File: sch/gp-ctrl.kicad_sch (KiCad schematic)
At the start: 10 parts

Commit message: more components
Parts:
- added A? (x2): SolderJumper_2_Open, Jumper:SolderJumper-2_P1.3mm_Open_TrianglePad1.0x1.5mm, symbol Jumper:SolderJumper_2_Open
- added D?: SS34, Diode_SMD:D_SMA, symbol Device:D_Schottky
- added Q?: 2N7002P, Package_TO_SOT_SMD:SOT-23, symbol Transistor_FET:2N7002
- added R? (x4): 10k, Resistor_SMD:R_0402_1005Metric_Pad0.72x0.64mm_HandSolder, symbol Device:R
- J?: LCSC (none) -> C3975165
- JP? (x3): footprint Jumper:SolderJumper-2_P1.3mm_Open_Pad1.0x1.5mm -> gpctrl:power_jumper
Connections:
- net +3V3: now also Q?.1 (G), R?.2
- net +5V: now also A?.2 (B), A?.2 (B), D?.1 (K), R?.2
- net GND: now also J?.14 (Pin_14), J?.20 (Pin_20), J?.30 (Pin_30), J?.34 (Pin_34), U?.6 (GND), R?.1, R?.1
- net at U?.1 (A1): now also A?.1 (A), R?.2, R?.2
- net at U?.2 (A0): now also A?.1 (A)
- net SDA1: now reaches U?.3 (SDA)
- net SCL1: now reaches U?.4 (SCL)
- net UART_P_RX: now reaches J?.10 (Pin_10)
- net SH_GP23_IMU: now reaches J?.16 (Pin_16)
- net SH_PGP24_IMU: now reaches J?.18 (Pin_18)
- net at J?.2 (Pin_2): now also J?.4 (Pin_4), D?.2 (A)
- net SDA_SH: now reaches J?.3 (Pin_3)
- net SCL_SH: now reaches J?.5 (Pin_5)
- net UART_P_TX: now reaches J?.8 (Pin_8)
- new net: Q?.3 (D), R?.1
- new net: Q?.2 (S), R?.1
- no-connect marks 0 -> 2
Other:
- sheet controller ports: added +5V, 3V3, GND, GPIO0, GPIO1, GPIO10, GPIO11, GPIO12, GPIO13, GPIO14, GPIO15, GPIO16, GPIO17, GPIO18, GPIO19, GPIO2, GPIO20, GPIO21, GPIO22, GPIO23_PICO_NO, GPIO24_PICO_NO, GPIO25_LED, GPIO26_ADC0, GPIO27_ADC1, GPIO28_ADC2, GPIO29_ADC3, GPIO3, GPIO4, GPIO5, GPIO6, GPIO7, GPIO8, GPIO9, RUN, SWCLK, SWD; removed none
- moved on the sheet: J?, JP?, K?, R?, U?

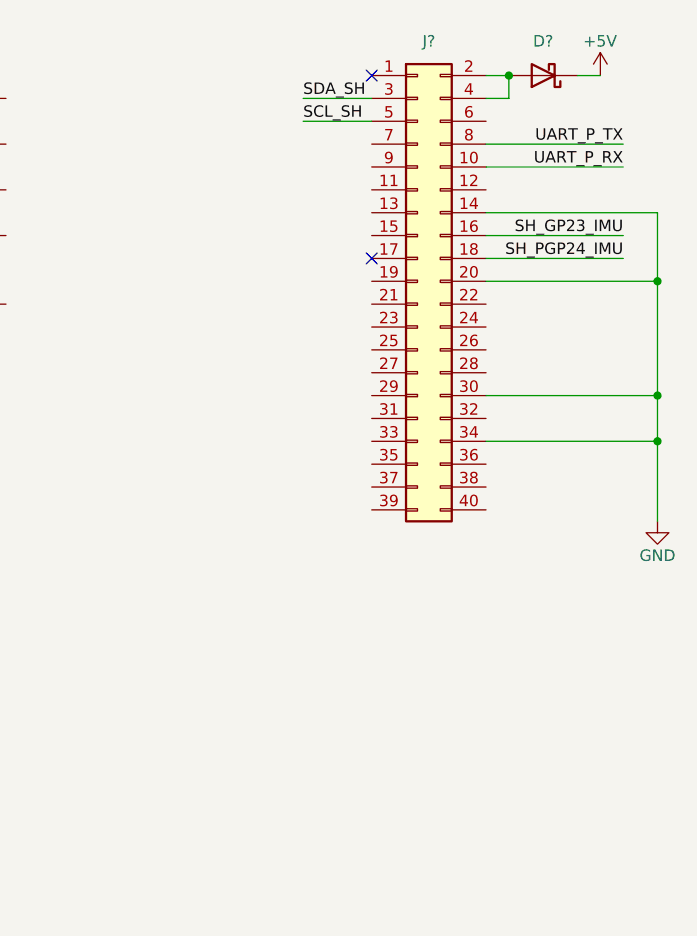
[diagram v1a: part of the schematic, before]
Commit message: updated downstream to sense hat connector
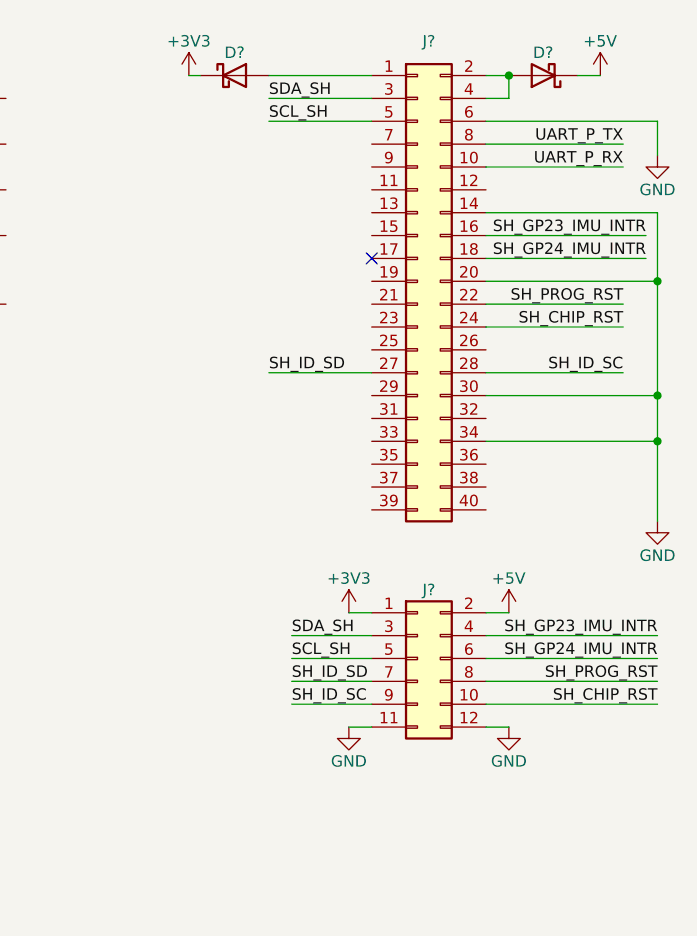
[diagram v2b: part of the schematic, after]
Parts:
- added D?: SS34, Diode_SMD:D_SMA, symbol Device:D_Schottky
- added J?: Conn_02x06_Odd_Even, Connector_PinHeader_2.54mm:PinHeader_2x06_P2.54mm_Horizontal, symbol Connector_Generic:Conn_02x06_Odd_Even
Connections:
- net +3V3: now also D?.1 (K), J?.1 (Pin_1)
- net +5V: now also J?.2 (Pin_2)
- net GND: now also J?.6 (Pin_6), J?.11 (Pin_11), J?.12 (Pin_12)
- net SCL_SH: now also J?.5 (Pin_5)
- net SDA_SH: now also J?.3 (Pin_3)
- net at J?.1 (Pin_1): now also D?.2 (A)
- net SH_PROG_RST: now reaches J?.22 (Pin_22)
- net SH_PROG_RST: now also J?.8 (Pin_8)
- net SH_CHIP_RST: now reaches J?.24 (Pin_24)
- net SH_CHIP_RST: now also J?.10 (Pin_10)
- net SH_ID_SD: now reaches J?.27 (Pin_27)
- net SH_ID_SD: now also J?.7 (Pin_7)
- net SH_ID_SC: now reaches J?.28 (Pin_28)
- net SH_ID_SC: now also J?.9 (Pin_9)
- net SH_GP23_IMU renamed SH_GP23_IMU_INTR
- net SH_GP23_IMU_INTR: now also J?.4 (Pin_4)
- net SH_PGP24_IMU renamed SH_GP24_IMU_INTR
- net SH_GP24_IMU_INTR: now also J?.6 (Pin_6)
- no-connect marks 2 -> 1

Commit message: sch update
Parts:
- added Q? (x3): 2N7002P, Package_TO_SOT_SMD:SOT-23, symbol Transistor_FET:2N7002
- added R? (x6): 10k, Resistor_SMD:R_0402_1005Metric_Pad0.72x0.64mm_HandSolder, symbol Device:R
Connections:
- net +3V3: now also Q?.1 (G), Q?.1 (G), Q?.1 (G), R?.2, R?.2, R?.2
- net +5V: now also R?.2, R?.2, R?.2
- new net: Q?.3 (D), R?.1 (x3)
- new net: Q?.2 (S), R?.1 (x3)
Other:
- note added: "1. No Board Sense"
- note added: "2. Board Sense Only"
- note added: "3. External Sense Only"
- moved on the sheet: A?, J?, JP?, K?, Q?, R?, U?

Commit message: sch update
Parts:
- removed K?: Relay_DPDT_Panasonic_AGQ200A4H, usb_xwitch:Relay_DPDT_Panasonic_AGQ200A4H, symbol usb_xwitch:Relay_DPDT_Panasonic_AGQ200A4H
- added J? (x2): 3.5mm_01x03, TerminalBlock_4Ucon:TerminalBlock_4Ucon_1x03_P3.50mm_Horizontal, symbol Connector:Screw_Terminal_01x03
- added J? (x2): DNP, Connector_PinHeader_2.54mm:PinHeader_1x03_P2.54mm_Vertical, symbol Connector_Generic:Conn_01x03
- added K? (x2): Relay_DPDT_Panasonic_AGQ200A4H, usb_xwitch:Relay_DPDT_Panasonic_AGQ200A4H, symbol usb_xwitch:Relay_DPDT_Panasonic_AGQ200A4H
- added Q? (x2): IRLML6244, Package_TO_SOT_SMD:SOT-23, symbol Transistor_FET:IRLML0030
- added R? (x2): 100K, Resistor_SMD:R_0603_1608Metric_Pad0.98x0.95mm_HandSolder, symbol Device:R
- added R?: 33K, Resistor_SMD:R_0603_1608Metric_Pad0.98x0.95mm_HandSolder, symbol Device:R
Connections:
- net at Q?.1 (G): now also Q?.3 (D), R?.1
- net at Q?.3 (D), R?.1: now also Q?.1 (G) (x3)
- new net: J?.3 (Pin_3), K?.2 (x2)
- new net: J?.1 (Pin_1), K?.3 (x2)
- new net: J?.2 (Pin_2), K?.4 (x2)
- new net: J?.2 (Pin_2), K?.5 (x2)
- new net: J?.1 (Pin_1), K?.6 (x2)
- new net: J?.3 (Pin_3), K?.7 (x2)
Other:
- note added: "Tri-Mode Current Sensor"
- moved on the sheet: Q?

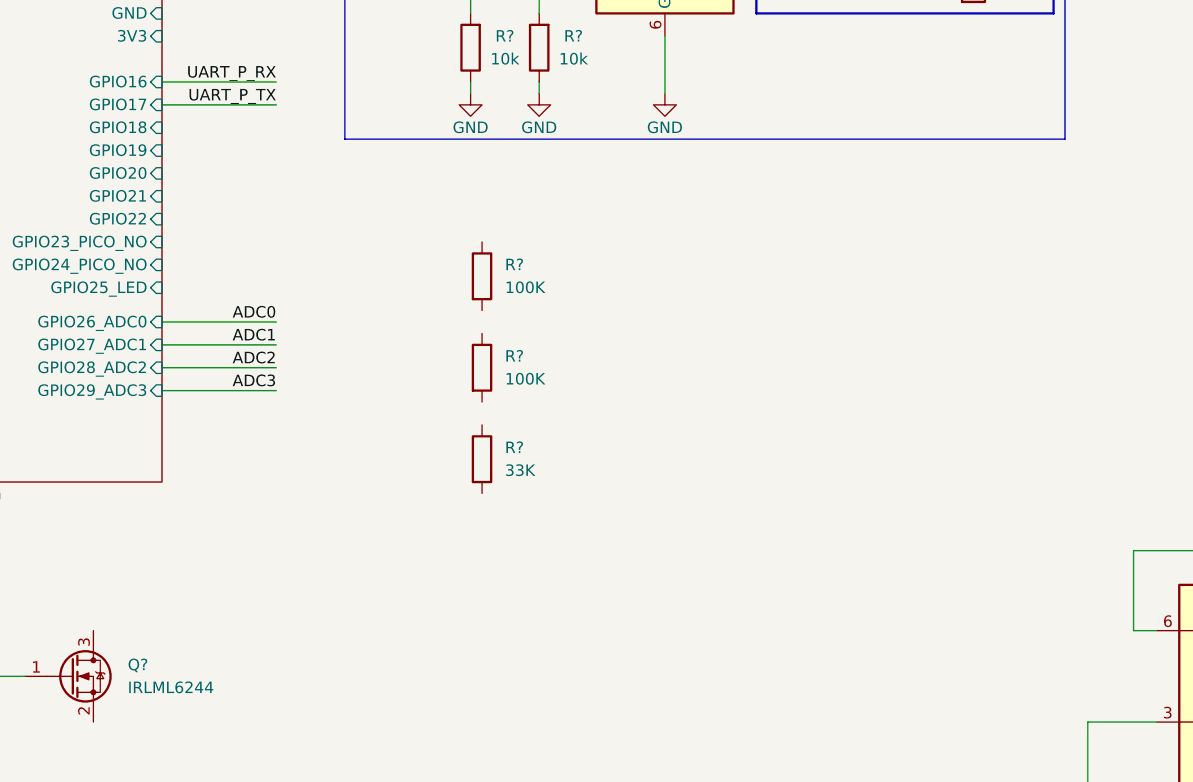
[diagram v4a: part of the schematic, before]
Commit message: adc added
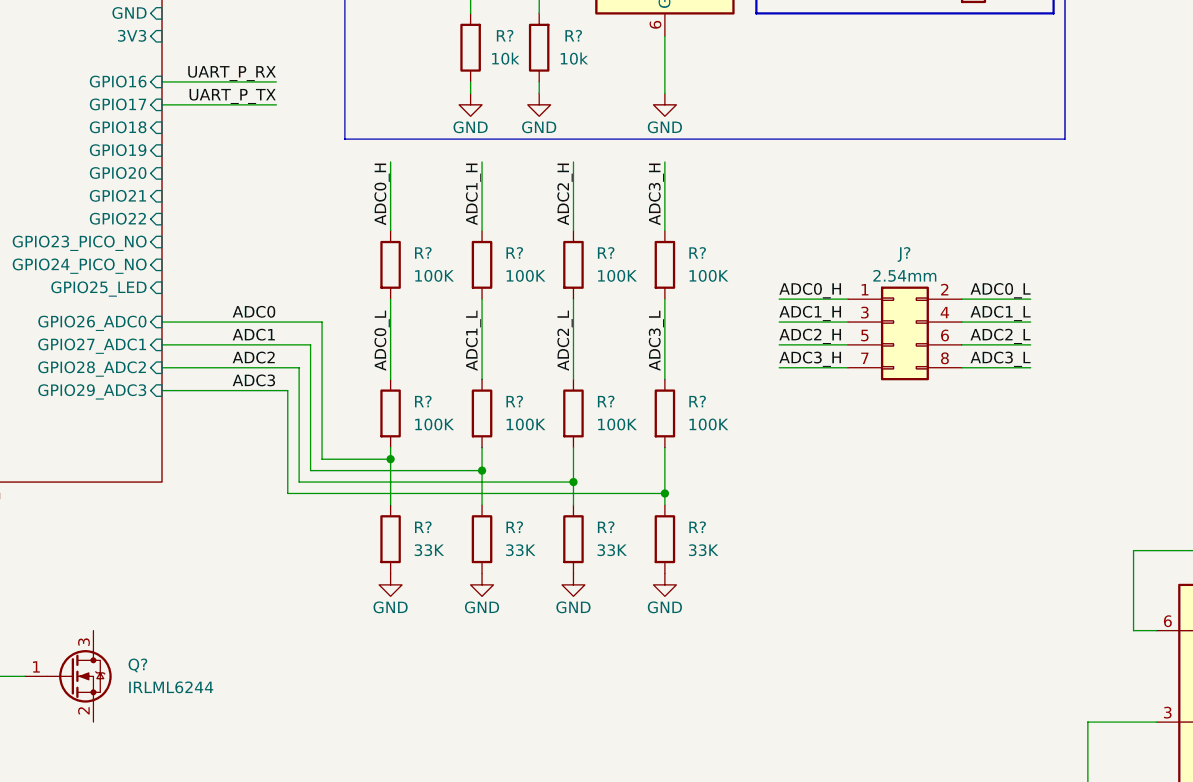
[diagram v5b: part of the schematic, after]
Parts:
- added J?: 2.54mm, Connector_PinHeader_2.54mm:PinHeader_2x04_P2.54mm_Vertical, symbol Connector_Generic:Conn_02x04_Odd_Even
- added R? (x6): 100K, Resistor_SMD:R_0603_1608Metric_Pad0.98x0.95mm_HandSolder, symbol Device:R
- added R? (x3): 33K, Resistor_SMD:R_0603_1608Metric_Pad0.98x0.95mm_HandSolder, symbol Device:R
- R? (x2): LCSC (none) -> C25803
- R?: LCSC (none) -> C4216
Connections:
- net ADC0: now also R?.1, R?.2
- net ADC1: now also R?.1, R?.2
- net ADC2: now also R?.1, R?.2
- net ADC3: now also R?.1, R?.2
- net GND: now also R?.2, R?.2, R?.2, R?.2
- net ADC3_L: now reaches R?.1
- net ADC3_L: now also R?.2, J?.8 (Pin_8)
- net ADC3_H: now reaches R?.1
- net ADC3_H: now also J?.7 (Pin_7)
- new net ADC0_H: J?.1 (Pin_1), R?.1
- new net ADC0_L: J?.2 (Pin_2), R?.1, R?.2
- new net ADC1_H: J?.3 (Pin_3), R?.1
- new net ADC1_L: J?.4 (Pin_4), R?.1, R?.2
- new net ADC2_H: J?.5 (Pin_5), R?.1
- new net ADC2_L: J?.6 (Pin_6), R?.1, R?.2
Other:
- moved on the sheet: R?

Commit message: sch and pcb layout update
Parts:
- removed J?: 3.5mm_01x03, TerminalBlock_4Ucon:TerminalBlock_4Ucon_1x03_P3.50mm_Horizontal, symbol Connector:Screw_Terminal_01x03
- removed J?: DNP, Connector_PinHeader_2.54mm:PinHeader_1x03_P2.54mm_Vertical, symbol Connector_Generic:Conn_01x03
- removed K?: Relay_DPDT_Panasonic_AGQ200A4H, usb_xwitch:Relay_DPDT_Panasonic_AGQ200A4H, symbol usb_xwitch:Relay_DPDT_Panasonic_AGQ200A4H
- added A1, A2: SolderJumper_2_Open, Jumper:SolderJumper-2_P1.3mm_Open_TrianglePad1.0x1.5mm, symbol Jumper:SolderJumper_2_Open
- added C1, C2: 100n, Resistor_SMD:R_0402_1005Metric_Pad0.72x0.64mm_HandSolder, symbol Device:C
- added D3, D4: B5819W SL, Diode_SMD:D_SOD-123, symbol Diode:BAT48ZFILM
- added H1, H2, H3, H4: RPI Mounting Hole, MountingHole:MountingHole_3.2mm_M3_Pad, symbol Mechanical:MountingHole
- added J1: DNP, Connector_PinHeader_2.54mm:PinHeader_1x02_P2.54mm_Vertical, symbol Connector_Generic:Conn_01x02
- added J10, J11, J13: 3.5mm, TerminalBlock_4Ucon:TerminalBlock_4Ucon_1x03_P3.50mm_Horizontal, symbol Connector:Screw_Terminal_01x03
- added J15: DNP, Connector_PinHeader_2.54mm:PinHeader_1x03_P2.54mm_Vertical_SMD_Pin1Left, symbol Connector_Generic:Conn_01x03
- added J16: Conn_02x06_Odd_Even, Connector_PinHeader_2.54mm:PinHeader_2x06_P2.54mm_Vertical, symbol Connector_Generic:Conn_02x06_Odd_Even
- added J5, J6, J9: 2.54mm, Connector_PinHeader_2.54mm:PinHeader_2x04_P2.54mm_Vertical, symbol Connector_Generic:Conn_02x04_Odd_Even
- added K2: Relay_DPDT_Panasonic_AGQ200A4H, usb_xwitch:Relay_DPDT_Panasonic_AGQ200A4H, symbol usb_xwitch:Relay_DPDT_Panasonic_AGQ200A4H
- added Q10, Q5, Q6, Q9: 2N7002P, Package_TO_SOT_SMD:SOT-23, symbol Transistor_FET:2N7002
- added R1, R2, R22, R27: 10K, Resistor_SMD:R_0603_1608Metric_Pad0.98x0.95mm_HandSolder, symbol Device:R
- added R3, R4: 100K, Resistor_SMD:R_0603_1608Metric_Pad0.98x0.95mm_HandSolder, symbol Device:R
- added SW1, SW2: C2689642, usb_xwitch:SW_SPST_CK_PTS636_SP43_SMTR, symbol Switch:SW_SPST
- J12: renamed from J?; value 3.5mm_01x03 -> 3.5mm
- J14: renamed from J?; footprint Connector_PinHeader_2.54mm:PinHeader_1x03_P2.54mm_Vertical -> Connector_PinHeader_2.54mm:PinHeader_1x03_P2.54mm_Vertical_SMD_Pin1Left
- J7: renamed from J?; LCSC (none) -> C225519
- J8: renamed from J?; value Conn_02x06_Odd_Even -> DNP; footprint Connector_PinHeader_2.54mm:PinHeader_2x06_P2.54mm_Horizontal -> Connector_PinHeader_2.54mm:PinHeader_2x06_P2.54mm_Vertical
- gave numbers to parts that had none: 42
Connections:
- net +12V: now also J9.1 (Pin_1), J9.2 (Pin_2)
- net +3V3: now also J5.7 (Pin_7), J5.8 (Pin_8), J6.7 (Pin_7), J6.8 (Pin_8), J9.5 (Pin_5), J9.6 (Pin_6), R1.1, R2.1, R22.1, R27.1
- net +5V: now also K1.1, D3.1 (K), D4.1 (K), J16.10 (Pin_10), J16.12 (Pin_12), J16.2 (Pin_2), J16.4 (Pin_4), J16.6 (Pin_6), J16.8 (Pin_8), J9.3 (Pin_3), J9.4 (Pin_4), K2.1
- net ADC0_H: now also J10.1 (Pin_1)
- net ADC0_L: now also J10.2 (Pin_2)
- net ADC1_H: now also J11.1 (Pin_1)
- net ADC1_L: now also J11.2 (Pin_2)
- net GND: now also J3.13 (Pin_13), J3.19 (Pin_19), J3.29 (Pin_29), J3.33 (Pin_33), J3.5 (Pin_5), Q12.2 (S), Q2.2 (S), Q4.2 (S), Q8.2 (S), C1.2, C2.2, J10.3 (Pin_3), J11.3 (Pin_3), J5.5 (Pin_5), J5.6 (Pin_6), J6.5 (Pin_5), J6.6 (Pin_6), J9.7 (Pin_7), J9.8 (Pin_8), Q10.2 (S), Q5.2 (S), Q6.2 (S), Q9.2 (S), R3.2, R4.2, SW1.1 (A), SW2.1 (A); no longer J3.14 (Pin_14), J3.20 (Pin_20), J3.30 (Pin_30), J3.34 (Pin_34), J3.6 (Pin_6)
- net SCL1: now also A1.1 (A), J5.2 (Pin_2), R2.2, R4.1
- net SCL_SH: now also J3.6 (Pin_6), A1.2 (B), J5.1 (Pin_1); no longer J3.5 (Pin_5)
- net SDA1: now also A2.1 (A), J5.4 (Pin_4), R1.2, R3.1
- net SDA_SH: now also J3.4 (Pin_4), A2.2 (B), J5.3 (Pin_3); no longer J3.3 (Pin_3)
- net SH_CHIP_RST: now also J3.23 (Pin_23); no longer J3.24 (Pin_24)
- net SH_GP23_IMU_INTR: now also J3.15 (Pin_15); no longer J3.16 (Pin_16)
- net SH_GP24_IMU_INTR: now also J3.17 (Pin_17); no longer J3.18 (Pin_18)
- net SH_ID_SC: now also J3.27 (Pin_27); no longer J3.28 (Pin_28)
- net SH_ID_SD: now also J3.28 (Pin_28); no longer J3.27 (Pin_27)
- net SH_PROG_RST: now also J3.21 (Pin_21); no longer J3.22 (Pin_22)
- net UART_P_RX: now also J3.9 (Pin_9); no longer J3.10 (Pin_10)
- net UART_P_TX: now also J3.7 (Pin_7); no longer J3.8 (Pin_8)
- net GP3: now reaches Q8.3 (D)
- net GP3: now also J16.5 (Pin_5)
- net at A4.1 (A), R6.2, U1.1 (A1): no longer R7.2
- net at A3.1 (A), U1.2 (A0): now also R7.2
- net GP2: now reaches Q4.3 (D)
- net GP2: now also J16.3 (Pin_3)
- net GP1: now reaches Q2.3 (D)
- net GP1: now also J16.1 (Pin_1)
- net CTGP4: now reaches Q11.2 (S), R28.1
- net CTGP2: now reaches Q3.2 (S), R23.1
- net CTGP1: now reaches Q1.2 (S), R20.1
- net at D1.2 (A): now also J3.2 (Pin_2); no longer J3.1 (Pin_1)
- net NC_RL_P0: now reaches J14.3 (Pin_3), K1.2
- net COM_RL_P0: now reaches J14.1 (Pin_1), K1.3
- net NO_RL_P0: now reaches J14.2 (Pin_2), K1.4
- net NO_RL_T0: now reaches J12.2 (Pin_2), K1.5
- net COM_RL_T0: now reaches J12.1 (Pin_1), K1.6
- net NC_RL_T0: now reaches J12.3 (Pin_3), K1.7
- net RL1: now reaches K1.8
- net RL1: now also D3.2 (A), Q5.3 (D)
- net CTGP3: now reaches Q7.2 (S), R25.1
- net GP4: now reaches Q12.3 (D)
- net GP4: now also J16.7 (Pin_7)
- new net: D2.2 (A), J3.1 (Pin_1), J3.3 (Pin_3)
- new net BTN1: C1.1, R22.2, SW1.2 (B)
- new net BTN2: C2.1, R27.2, SW2.2 (B)
- new net COM_RL_P1: J15.1 (Pin_1), K2.3
- new net COM_RL_T1: J13.1 (Pin_1), K2.6
- new net CTGP5: Q6.1 (G)
- new net CTGP6: Q10.1 (G)
- new net GP5: J16.9 (Pin_9), Q6.3 (D)
- new net GP6: J16.11 (Pin_11), Q10.3 (D)
- new net MI_RX: J6.1 (Pin_1)
- new net MO_TX: J6.2 (Pin_2)
- new net NC_RL_P1: J15.3 (Pin_3), K2.2
- new net NC_RL_T1: J13.3 (Pin_3), K2.7
- new net NO_RL_P1: J15.2 (Pin_2), K2.4
- new net NO_RL_T1: J13.2 (Pin_2), K2.5
- new net RL1_CTL: Q5.1 (G)
- new net RL2: D4.2 (A), K2.8, Q9.3 (D)
- new net RL2_CTL: Q9.1 (G)
- new net SCK_SP: J6.3 (Pin_3)
- new net SCL_CS: J6.4 (Pin_4)
- new net UART0_RX: J1.1 (Pin_1)
- new net UART0_TX: J1.2 (Pin_2)
- no-connect marks 1 -> 29
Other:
- note added: "ADC 4ch"
- note added: "Buttons x2"
- note added: "General Purpose Control"
- note added: "I2C x2"
- note added: "IO"
- note added: "Relay x2"
- note added: "SPI x1"
- note added: "merge i2c buses"
- note added: "sense hat downstream"
- moved on the sheet: A3, A4, J12, J14, J4, J7, JP1, JP2, JP3, K1, Q1, Q11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
